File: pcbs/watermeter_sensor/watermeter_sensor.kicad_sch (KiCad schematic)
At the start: 14 parts, among them J1 Conn_01x06, U1 LDC2112, U2 MCP1811A

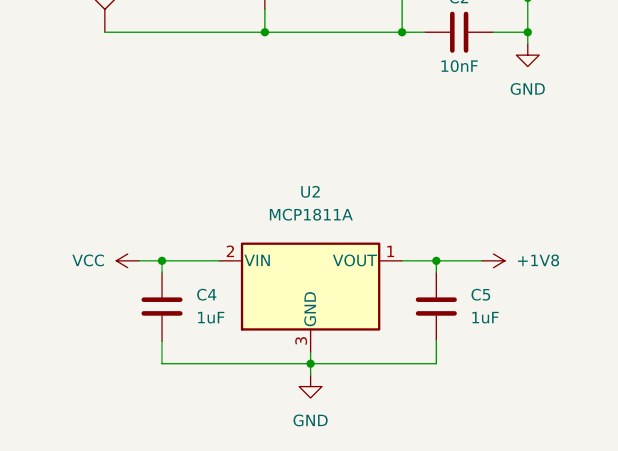
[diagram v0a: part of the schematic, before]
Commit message: PCB Changes v1.1: - changed LDO - some footprints changed to 0603
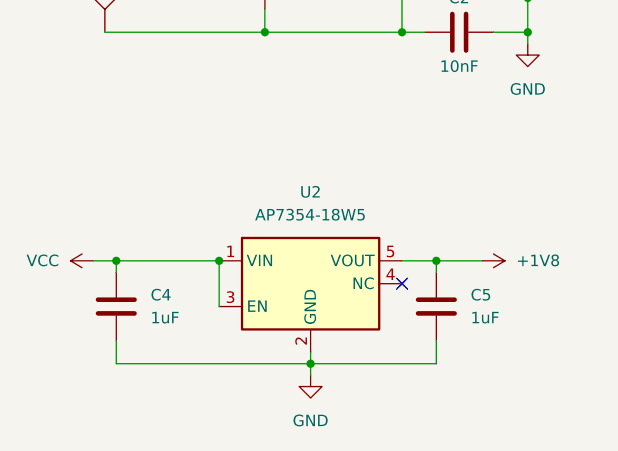
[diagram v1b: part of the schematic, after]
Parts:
- removed U2: MCP1811A, Package_TO_SOT_SMD:SOT-23, symbol Regulator_Linear_Goodies:MCP1811A
- added U2: AP7354-18W5, Package_TO_SOT_SMD:TSOT-23-5, symbol Regulator_Linear:ADP7142AUJZ-1.8
- C1, C3: BOM (none) -> C0G 5% 50V
- C4: footprint Capacitor_SMD:C_0805_2012Metric -> Capacitor_SMD:C_0603_1608Metric
- C5: footprint Capacitor_SMD:C_0805_2012Metric -> Capacitor_SMD:C_0603_1608Metric; BOM (none) -> X7R 10% 6.3V
- R1, R2: footprint Resistor_SMD:R_0805_2012Metric -> Resistor_SMD:R_0603_1608Metric
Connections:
- net +1V8: now also U2.5 (VOUT)
- net GND: now also U2.2 (GND)
- net VCC: now also U2.1 (VIN), U2.3 (EN)
- no-connect marks 1 -> 2
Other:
- moved on the sheet: C4
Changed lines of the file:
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@@
 	)
 	(junction
-		(at 69.85 132.08)
+		(at 64.77 132.08)
 		(diameter 0)
 		(color 0 0 0 0)
@@
 	)
 	(junction
+		(at 76.2 132.08)
+		(diameter 0)
+		(color 0 0 0 0)
+	)
+	(junction
 		(at 96.52 106.68)
 		(diameter 0)
@@
 		(at 124.46 85.09)
 	)
+	(no_connect
+		(at 96.52 134.62)
+	)
 	(wire
 		(pts
@@
 	(wire
 		(pts
-			(xy 69.85 132.08) (xy 69.85 133.35)
+			(xy 64.77 132.08) (xy 64.77 133.35)
 		)
 		(stroke
@@
 	(wire
 		(pts
-			(xy 69.85 143.51) (xy 86.36 143.51)
-		)
-		(stroke
-			(width 0)
-			(type default)
-		)
-	)
-	(wire
-		(pts
-			(xy 69.85 140.97) (xy 69.85 143.51)
+			(xy 64.77 143.51) (xy 86.36 143.51)
+		)
+		(stroke
+			(width 0)
+			(type default)
+		)
+	)
+	(wire
+		(pts
+			(xy 64.77 140.97) (xy 64.77 143.51)
 		)
 		(stroke
@@
 	(wire
 		(pts
+			(xy 76.2 132.08) (xy 76.2 137.16)
+		)
+		(stroke
+			(width 0)
+			(type default)
+		)
+	)
+	(wire
+		(pts
 			(xy 110.49 102.87) (xy 110.49 106.68)
 		)
@@
 	(wire
 		(pts
-			(xy 69.85 132.08) (xy 76.2 132.08)
-		)
-		(stroke
-			(width 0)
-			(type default)
-		)
-	)
-	(wire
-		(pts
-			(xy 67.31 132.08) (xy 69.85 132.08)
+			(xy 64.77 132.08) (xy 76.2 132.08)
+		)
+		(stroke
+			(width 0)
+			(type default)
+		)
+	)
+	(wire
+		(pts
+			(xy 62.23 132.08) (xy 64.77 132.08)
 		)
 		(stroke
@@
 			)
 		)
-		(property "Footprint" "Resistor_SMD:R_0805_2012Metric"
+		(property "Footprint" "Resistor_SMD:R_0603_1608Metric"
 			(at 146.812 85.09 90)
 			(effects
@@
 			)
 		)
-		(property "Description" ""
+		(property "Description" "5%"
 			(at 148.59 85.09 0)
 			(effects
@@
 	)
 	(symbol
-		(lib_id "Regulator_Linear_Goodies:MCP1811A")
-		(at 86.36 134.62 0)
-		(unit 1)
-		(exclude_from_sim no)
-		(in_bom yes)
-		(on_board yes)
-		(dnp no)
-		(fields_autoplaced yes)
-		(property "Reference" "U2"
-			(at 86.36 124.46 0)
-			(effects
-				(font
-					(size 1.27 1.27)
-				)
-			)
-		)
-		(property "Value" "MCP1811A"
-			(at 86.36 127 0)
-			(effects
-				(font
-					(size 1.27 1.27)
-				)
-			)
-		)
-		(property "Footprint" "Package_TO_SOT_SMD:SOT-23"
-			(at 86.36 127 0)
-			(effects
-				(font
-					(size 1.27 1.27)
-				)
-				(hide yes)
-			)
-		)
-		(property "Datasheet" "https://www.microchip.com/content/dam/mchp/documents/APID/ProductDocuments/DataSheets/MCP1811A-11B-12A-12B-Family-Data-Sheet-DS20006088C.pdf"
-			(at 86.36 134.62 0)
-			(effects
-				(font
-					(size 1.27 1.27)
-				)
-				(hide yes)
-			)
-		)
-		(property "Description" ""
-			(at 86.36 134.62 0)
-			(effects
-				(font
-					(size 1.27 1.27)
-				)
-				(hide yes)
-			)
-		)
-		(pin "1"
-		)
-		(pin "2"
-		)
-		(pin "3"
-		)
-		(pin "3"
-		)
-		(instances
-			(project ""
-				(path "/afaee055-9392-4ae6-aa7e-cc2770462548"
-					(reference "U2")
-					(unit 1)
-				)
-			)
-		)
-	)
-	(symbol
 		(lib_id "power:+1V8")
 		(at 111.76 73.66 0)
@@
 	(symbol
 		(lib_id "power:VCC")
-		(at 67.31 132.08 90)
+		(at 62.23 132.08 90)
 		(unit 1)
 		(exclude_from_sim no)
@@
 		(fields_autoplaced yes)
 		(property "Reference" "#PWR01"
-			(at 71.12 132.08 0)
+			(at 66.04 132.08 0)
 			(effects
 				(font
@@
 		)
 		(property "Value" "VCC"
-			(at 63.5 132.0799 90)
+			(at 58.42 132.0799 90)
 			(effects
 				(font
@@
 		)
 		(property "Footprint" ""
-			(at 67.31 132.08 0)
+			(at 62.23 132.08 0)
 			(effects
 				(font
@@
 		)
 		(property "Datasheet" ""
-			(at 67.31 132.08 0)
+			(at 62.23 132.08 0)
 			(effects
 				(font
@@
 		)
 		(property "Description" ""
-			(at 67.31 132.08 0)
+			(at 62.23 132.08 0)
 			(effects
 				(font
@@
 			)
 		)
-		(property "Description" ""
+		(property "Description" "C0G 5% 50V"
+			(at 81.28 82.55 0)
+			(effects
+				(font
+					(size 1.27 1.27)
+				)
+				(hide yes)
+			)
+		)
+		(property "BOM" "C0G 5% 50V"
 			(at 81.28 82.55 0)
 			(effects
@@
 				(path "/afaee055-9392-4ae6-aa7e-cc2770462548"
 					(reference "C1")
+					(unit 1)
+				)
+			)
+		)
+	)
+	(symbol
+		(lib_id "Regulator_Linear:ADP7142AUJZ-1.8")
+		(at 86.36 134.62 0)
+		(unit 1)
+		(exclude_from_sim no)
+		(in_bom yes)
+		(on_board yes)
+		(dnp no)
+		(fields_autoplaced yes)
+		(property "Reference" "U2"
+			(at 86.36 124.46 0)
+			(effects
+				(font
+					(size 1.27 1.27)
+				)
+			)
+		)
+		(property "Value" "AP7354-18W5"
+			(at 86.36 127 0)
+			(effects
+				(font
+					(size 1.27 1.27)
+				)
+			)
+		)
+		(property "Footprint" "Package_TO_SOT_SMD:TSOT-23-5"
+			(at 86.36 144.78 0)
+			(effects
+				(font
+					(size 1.27 1.27)
+					(italic yes)
+				)
+				(hide yes)
+			)
+		)
+		(property "Datasheet" "https://nl.mouser.com/datasheet/2/115/DIOD_S_A0010206046_1-2543502.pdf"
+			(at 86.36 147.32 0)
+			(effects
+				(font
+					(size 1.27 1.27)
+				)
+				(hide yes)
+			)
+		)
+		(property "Description" "150mA, Low Noise, CMOS Low Dropout Regulator, Positive, 1.8V Fixed Output, TSOT-23-5"
+			(at 86.36 134.62 0)
+			(effects
+				(font
+					(size 1.27 1.27)
+				)
+				(hide yes)
+			)
+		)
+		(property "BOM" ""
+			(at 86.36 134.62 0)
+			(effects
+				(font
+					(size 1.27 1.27)
+				)
+				(hide yes)
+			)
+		)
+		(pin "5"
+		)
+		(pin "4"
+		)
+		(pin "2"
+		)
+		(pin "1"
+		)
+		(pin "3"
+		)
+		(instances
+			(project ""
+				(path "/afaee055-9392-4ae6-aa7e-cc2770462548"
+					(reference "U2")
 					(unit 1)
 				)
@@
 			)
 		)
-		(property "Footprint" "Capacitor_SMD:C_0805_2012Metric"
+		(property "Footprint" "Capacitor_SMD:C_0603_1608Metric"
 			(at 101.2952 140.97 0)
 			(effects
@@
 			)
 		)
-		(property "Description" ""
+		(property "Description" "X7R 10% 6.3V"
+			(at 100.33 137.16 0)
+			(effects
+				(font
+					(size 1.27 1.27)
+				)
+				(hide yes)
+			)
+		)
+		(property "BOM" "X7R 10% 6.3V"
 			(at 100.33 137.16 0)
 			(effects
@@
 			)
 		)
-		(property "Footprint" "Resistor_SMD:R_0805_2012Metric"
+		(property "Footprint" "Resistor_SMD:R_0603_1608Metric"
 			(at 136.652 85.09 90)
 			(effects
@@
 			)
 		)
-		(property "Description" ""
+		(property "Description" "5%"
 			(at 138.43 85.09 0)
 			(effects
@@
 			)
 		)
-		(property "Description" ""
+		(property "Description" "X7R 5% 50V"
 			(at 102.87 106.68 0)
 			(effects
@@
 	(symbol
 		(lib_id "Device:C")
-		(at 69.85 137.16 0)
+		(at 64.77 137.16 0)
 		(unit 1)
 		(exclude_from_sim no)
@@
 		(fields_autoplaced yes)
 		(property "Reference" "C4"
-			(at 73.66 135.8899 0)
+			(at 68.58 135.8899 0)
 			(effects
 				(font
@@
 		)
 		(property "Value" "1uF"
-			(at 73.66 138.4299 0)
+			(at 68.58 138.4299 0)
 			(effects
 				(font
@@
 			)
 		)
-		(property "Footprint" "Capacitor_SMD:C_0805_2012Metric"
-			(at 70.8152 140.97 0)
+		(property "Footprint" "Capacitor_SMD:C_0603_1608Metric"
+			(at 65.7352 140.97 0)
 			(effects
 				(font
@@
 		)
 		(property "Datasheet" "~"
-			(at 69.85 137.16 0)
-			(effects
-				(font
-					(size 1.27 1.27)
-				)
-				(hide yes)
-			)
-		)
-		(property "Description" ""
-			(at 69.85 137.16 0)
+			(at 64.77 137.16 0)
+			(effects
+				(font
+					(size 1.27 1.27)
+				)
+				(hide yes)
+			)
+		)
+		(property "Description" "X7R 10% 6.3V"
+			(at 64.77 137.16 0)
 			(effects
 				(font
@@
 			)
 		)
-		(property "Description" ""
+		(property "Description" "C0G 5% 50V"
 			(at 81.28 100.33 0)
 			(effects
+				(font
+					(size 1.27 1.27)
+				)
+				(hide yes)
+			)
+		)
+		(property "BOM" "C0G 5% 50V"
+			(at 81.28 100.33 0)
+			(effects
